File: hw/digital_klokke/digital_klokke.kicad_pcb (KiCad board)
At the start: 2 copper layers, 13 parts, among them SW101 SW_Push, SW102 SW_Push, SW103 SW_Push, U201 74LS47

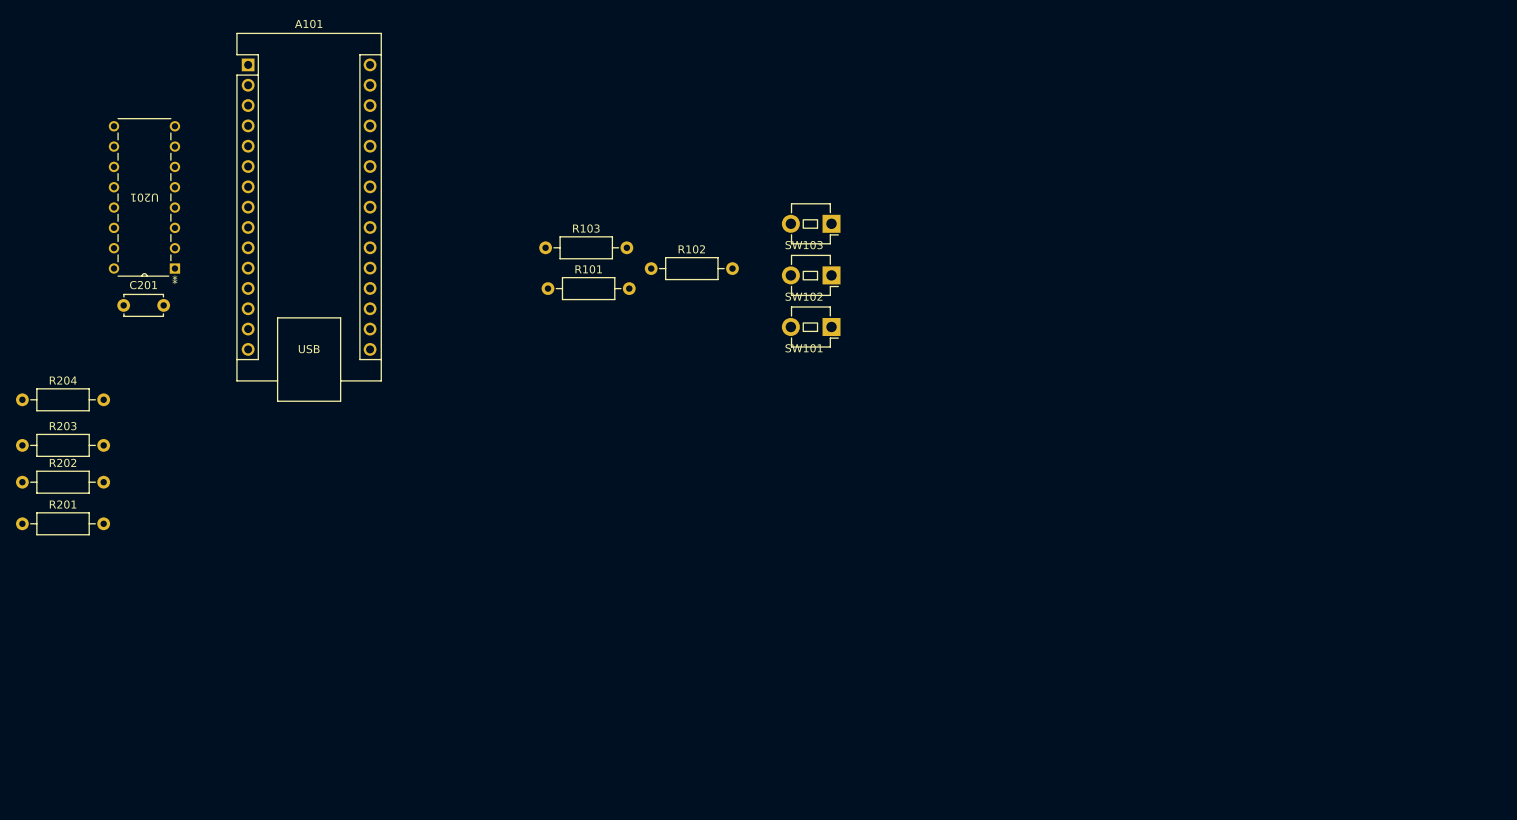
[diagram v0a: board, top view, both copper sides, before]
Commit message: added led for power indication. Started routing
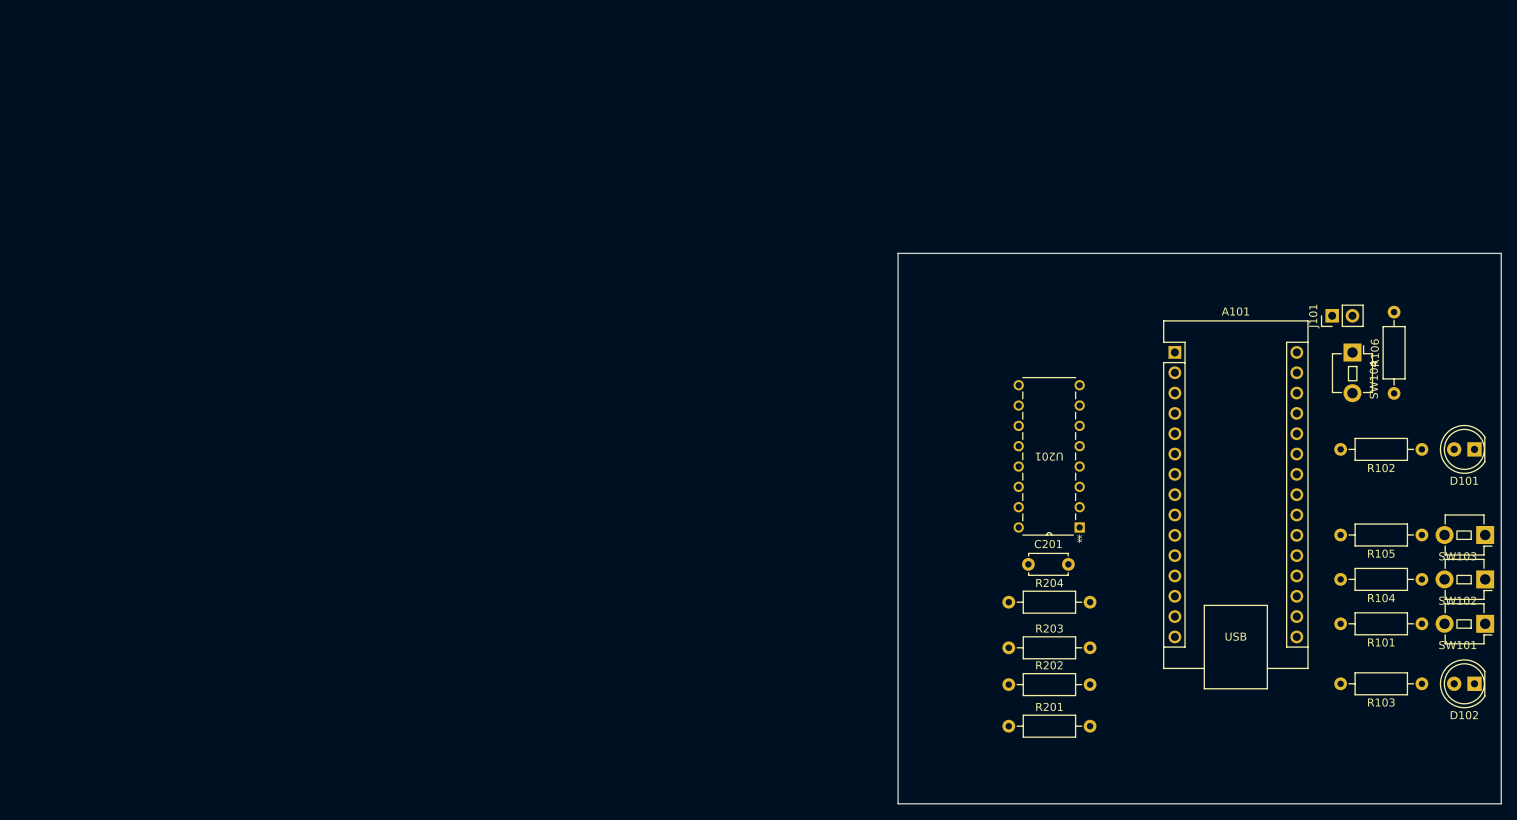
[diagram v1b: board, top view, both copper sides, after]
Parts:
- added D101: green, LED_THT:LED_D5.0mm, F.Cu at (210.4, 108.6)
- added D102: green, LED_THT:LED_D5.0mm, F.Cu at (210.4, 137.9)
- added J101: Conn_01x02_Pin, Connector_PinHeader_2.54mm:PinHeader_1x02_P2.54mm_Vertical, F.Cu at (192.6, 91.9)
- added R104: 1k, Resistor_THT:R_Axial_DIN0207_L6.3mm_D2.5mm_P10.16mm_Horizontal, F.Cu at (203.8, 124.8)
- added R105: 1k, Resistor_THT:R_Axial_DIN0207_L6.3mm_D2.5mm_P10.16mm_Horizontal, F.Cu at (203.8, 119.3)
- added R106: 1k, Resistor_THT:R_Axial_DIN0207_L6.3mm_D2.5mm_P10.16mm_Horizontal, F.Cu at (200.3, 101.6)
- added SW104: SW_Push, OMG_Switches:SW_PUSH_1P1T_6x3.5mm_H5.0_APEM_MJTP1250, F.Cu at (195.1, 96.5)
- R102: value 1k -> 270
- R103: value 1k -> 75
- moved R201 125.9 mm to (152.1, 143.2)
- moved R202 125.9 mm to (152.1, 138.0)
- moved R203 125.9 mm to (152.1, 133.4)
- moved R204 125.9 mm to (152.1, 127.7)
- moved R103 122.3 mm to (203.8, 137.9), turned to 180 degrees
- moved A101 121.3 mm to (172.9, 96.5)
- moved C201 117.6 mm to (154.6, 123.0)
- moved U201 117.6 mm to (153.4, 100.6)
- moved R101 117.0 mm to (203.8, 130.4), turned to 180 degrees
- moved R102 99.0 mm to (203.8, 108.6), turned to 180 degrees
- moved SW103 90.5 mm to (211.7, 119.3)
- moved SW102 90.1 mm to (211.7, 124.8)
- moved SW101 89.7 mm to (211.7, 130.4)
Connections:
- A101 pad 17: unconnected-(A101-3V3-Pad17) -> +3V3
- A101 pad 28: unconnected-(A101-~{RESET}-Pad28) -> /nRST
- A101 pad 3: unconnected-(A101-~{RESET}-Pad3) -> /nRST
- R102 pad 1: /Decrease_time -> Net-(D101-A)
- R102 pad 2: GND -> +5V
- R103 pad 1: /Adjust -> Net-(D102-A)
- R103 pad 2: GND -> +3V3
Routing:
- added copper zone on In2.Cu, net +5V
- added copper zone on In1.Cu, net GND
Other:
- board outline added: 75.4 x 68.8 mm
- copper layers 2 -> 4

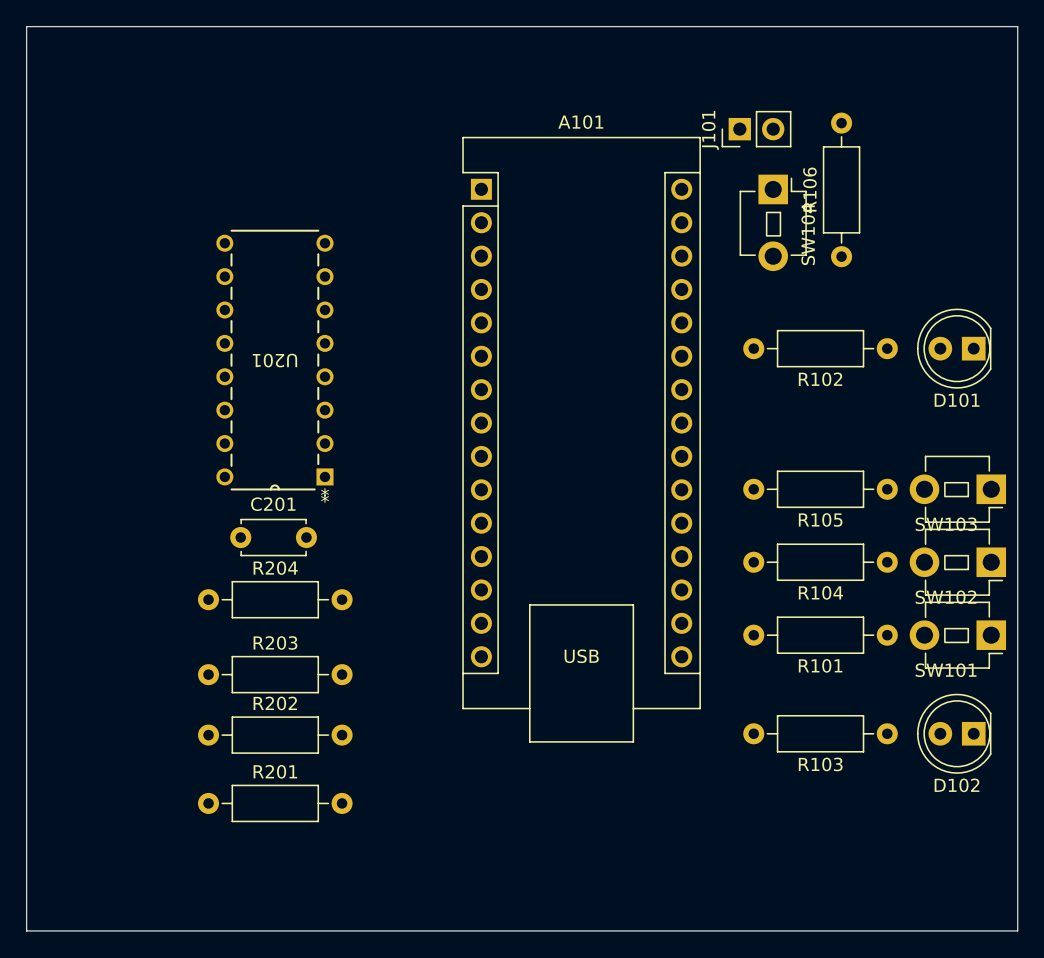
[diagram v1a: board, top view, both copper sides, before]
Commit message: added segment display footprint
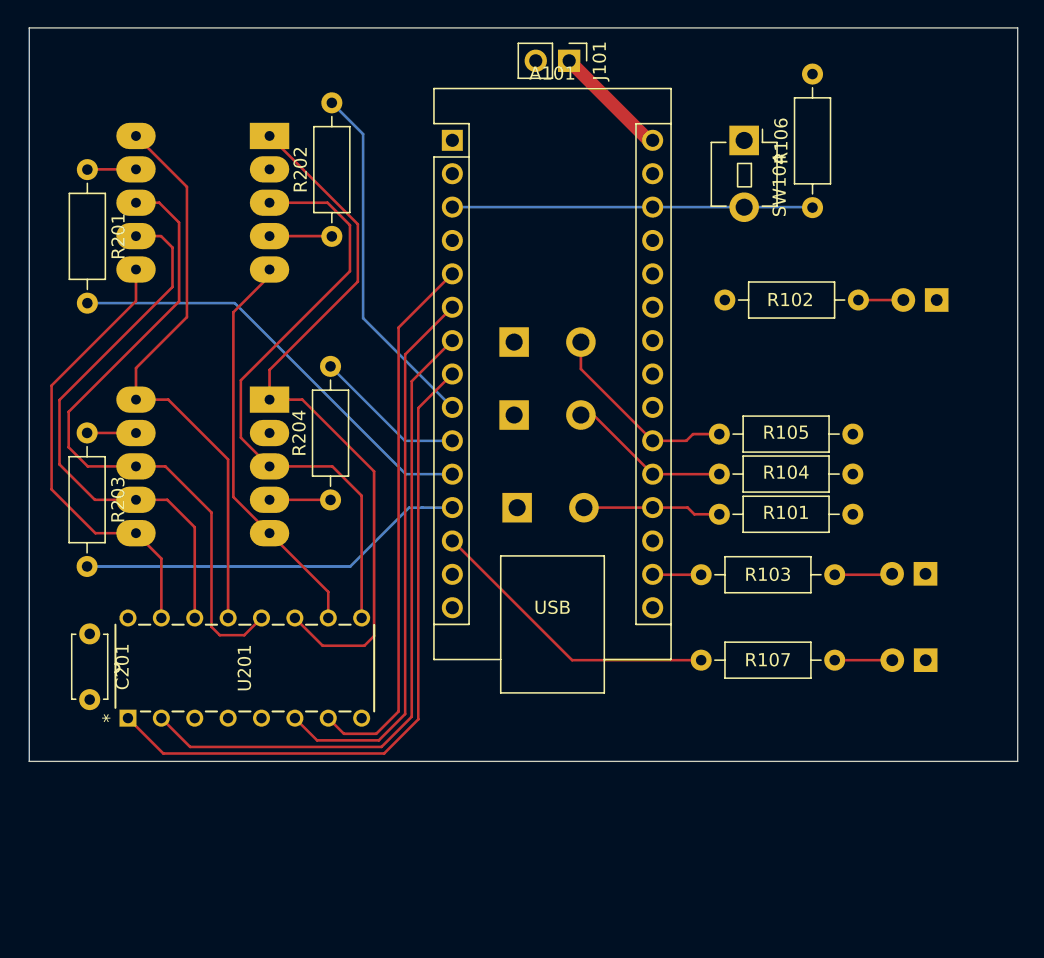
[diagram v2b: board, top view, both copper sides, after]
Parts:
- added D103: green, LED_THT:LED_D5.0mm, B.Cu at (206.7, 132.3)
- added D201: LTD-4608JF, OMG_Optoelectronics:Lite-On LTD-4608JF, B.Cu at (151.7, 97.5)
- added D202: LTD-4608JF, OMG_Optoelectronics:Lite-On LTD-4608JF, B.Cu at (151.7, 117.6)
- added R107: 270, Resistor_THT:R_Axial_DIN0207_L6.3mm_D2.5mm_P10.16mm_Horizontal, F.Cu at (199.8, 132.3)
- D101, D102, SW101, SW102, SW103: moved to B.Cu
- moved R201 49.1 mm to (142.9, 95.0), turned to -90 degrees
- moved R202 39.1 mm to (161.5, 100.1), turned to 90 degrees
- moved SW103 38.0 mm to (175.4, 108.1), turned to 0 degrees
- moved SW102 38.0 mm to (175.4, 113.7), turned to 0 degrees
- moved SW101 37.4 mm to (175.6, 120.7), turned to 0 degrees
- moved U201 30.4 mm to (163.8, 129.1), turned to 90 degrees
- moved R203 20.6 mm to (142.9, 115.0), turned to -90 degrees
- moved R101 15.7 mm to (191.0, 121.2), turned to 0 degrees
- moved R104 14.4 mm to (191.0, 118.1), turned to 0 degrees
- moved J101 14.0 mm to (179.6, 86.7), turned to -90 degrees
- moved C201 13.6 mm to (143.1, 130.3), turned to -90 degrees
- moved R105 13.5 mm to (191.0, 115.1), turned to 0 degrees
- moved R103 12.7 mm to (199.8, 125.8)
- moved D102 12.7 mm to (206.7, 125.7)
- moved R204 12.0 mm to (161.4, 120.1), turned to 90 degrees
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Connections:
- net /seven_segment/A renamed /A
- net /seven_segment/B renamed /B
- net /seven_segment/C renamed /C
- net /seven_segment/D renamed /D
- A101 pad 10: /seven_segment/Minutes_ones -> /Minutes_tens
- A101 pad 11: /seven_segment/Seconds_tens -> /Seconds_ones
- A101 pad 12: /seven_segment/Seconds_ones -> /Minutes_ones
- A101 pad 13: unconnected-(A101-D10-Pad13) -> /config_led
- A101 pad 9: /seven_segment/Minutes_tens -> /Seconds_tens
- R201 pad 2: /seven_segment/Seconds_ones -> /Seconds_ones
- R202 pad 2: /seven_segment/Seconds_tens -> /Seconds_tens
- R203 pad 2: /seven_segment/Minutes_ones -> /Minutes_ones
- R204 pad 2: /seven_segment/Minutes_tens -> /Minutes_tens
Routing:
- net Net-(D201-C): track 0.00 -> 55.6 mm
- net /B: track 0.00 -> 51.6 mm
- net /C: track 0.00 -> 50.8 mm
- net Net-(D201-B): track 0.00 -> 50.7 mm
- net Net-(D201-E): track 0.00 -> 46.8 mm
- net Net-(D201-A): track 0.00 -> 44.2 mm
- net Net-(D201-G): track 0.00 -> 42.4 mm
- net /D: track 0.00 -> 42.4 mm
- net /A: track 0.00 -> 41.5 mm
- net Net-(D201-F): track 0.00 -> 34.4 mm
- net /Seconds_ones: track 0.00 -> 33.2 mm
- net Net-(D201-D): track 0.00 -> 30.6 mm
- net /Minutes_ones: track 0.00 -> 29.6 mm
- net /nRST: track 0.00 -> 27.4 mm
- net /Seconds_tens: track 0.00 -> 27.0 mm
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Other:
- board size 75.4 x 68.8 mm -> 75.2 x 55.8 mm

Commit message: final design changes. Design freeze
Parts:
- removed D103: green, LED_THT:LED_D5.0mm
- removed R107: 270, Resistor_THT:R_Axial_DIN0207_L6.3mm_D2.5mm_P10.16mm_Horizontal
- added H101: MountingHole, MountingHole:MountingHole_4.3mm_M4, F.Cu at (348.5, 94.1)
- added H102: MountingHole, MountingHole:MountingHole_4.3mm_M4, F.Cu at (312.8, 135.2)
- moved SW101 164.6 mm to (340.2, 116.9), turned to 90 degrees
- moved SW102 158.5 mm to (333.9, 116.9), turned to 90 degrees
- moved SW103 152.5 mm to (327.6, 116.9), turned to 90 degrees
- moved R101 150.9 mm to (340.7, 102.5), turned to 90 degrees
- moved R104 147.5 mm to (337.6, 102.5), turned to 90 degrees
- moved A101 144.7 mm to (312.2, 122.9), turned to 90 degrees
- moved R105 144.1 mm to (334.6, 102.5), turned to 90 degrees
- moved R202 142.9 mm to (304.3, 104.4)
- moved C201 142.9 mm to (285.9, 134.6)
- moved D201 142.9 mm to (294.5, 101.8)
- moved D202 142.9 mm to (294.5, 121.9)
- moved R201 142.9 mm to (285.7, 99.3)
- moved R203 142.9 mm to (285.7, 119.3)
- moved R204 142.9 mm to (304.2, 124.4)
- moved U201 142.9 mm to (306.6, 133.4)
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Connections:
- D201 pad 2: +5V -> /config_led
- D202 pad 2: +5V -> /config_led
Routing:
- net /Minutes_ones: track 29.6 -> 117.1 mm
- net /Seconds_ones: track 33.2 -> 91.6 mm
- net /config_led: track 22.7 -> 76.0 mm
- net /Seconds_tens: track 27.0 -> 57.0 mm
- net +3V3: track 3.70 -> 30.9 mm
- net /Minutes_tens: track 11.6 -> 34.5 mm
- net /A: track 41.5 -> 32.7 mm
- net +9V: track 8.86 -> 16.6 mm
- net /B: track 51.6 -> 56.9 mm
- net Net-(D103-A): track 4.38 -> 0.00 mm
- net /D: track 42.4 -> 38.3 mm
- net +5V: track 0.00 -> 3.41 mm
- net Net-(D201-C): track 55.6 -> 57.5 mm
- net /nRST: track 27.4 -> 25.7 mm
- net /Decrease_time: track 12.4 -> 10.9 mm
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- added copper zone on B.Cu, net GND
- added copper zone on F.Cu, net GND
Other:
- board size 75.2 x 55.8 mm -> 73.1 x 55.8 mm
- board text added: "${TITLE} - ${REVISION}"
- board text added: "0"
- board text added: "0 mm"
- board text added: "0.0000 mm / 0.0000 mm"
- board text added: "0.01 mm"
- board text added: "0.02"
- board text added: "0.035 mm"
- board text added: "0.1 mm"
- board text added: "0.3000 mm"
- board text added: "1"
- board text added: "1.24 mm"
- board text added: "1.6000 mm"
- board text added: "3.3"
- board text added: "4"
- board text added: "4.5"
- board text added: "73.1000 mm x 55.8000 mm"
- board text added: "@omg_vustah"
- board text added: "B.Mask"
- board text added: "B.Paste"
- board text added: "B.Silkscreen"
- board text added: "BOARD CHARACTERISTICS"
- board text added: "Board Thickness:"
- board text added: "Board overall dimensions:"
- board text added: "Bottom Silk Screen"
- board text added: "Bottom Solder Mask"
- board text added: "Bottom Solder Paste"
- board text added: "Castellated pads:"
- board text added: "Color"
- board text added: "Copper Finish:"
- board text added: "Copper Layer Count:"
- board text added: "Dielectric 1"
- board text added: "Dielectric 2"
- board text added: "Dielectric 3"
- board text added: "Edge card connectors:"
- board text added: "Epsilon R"
- board text added: "F.Mask"
- board text added: "F.Paste"
- board text added: "F.Silkscreen"
- board text added: "FR4"
- board text added: "Impedance Control:"
- board text added: "L1_top"
- board text added: "L2_GND"
- board text added: "L3_PWR"
- board text added: "L4_bot"
- board text added: "Layer Name"
- board text added: "Loss Tangent"
- board text added: "Material"
- board text added: "Min hole diameter:"
- board text added: "Min track/spacing:"
- board text added: "No"
- board text added: "None"
- board text added: "Not specified"
- board text added: "Ole M.G. Vister"
- board text added: "Plated Board Edge:"
- board text added: "Thickness (mm)"
- board text added: "Top Silk Screen"
- board text added: "Top Solder Mask"
- board text added: "Top Solder Paste"
- board text added: "Type"
- board text added: "copper"
- board text added: "core"
- board text added: "prepreg"

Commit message: added resistor to each cathode
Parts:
- added R205: 470, Resistor_SMD:R_0805_2012Metric_Pad1.20x1.40mm_HandSolder, F.Cu at (304.2, 101.8)
- added R206: 470, Resistor_SMD:R_0805_2012Metric_Pad1.20x1.40mm_HandSolder, F.Cu at (284.9, 106.9)
- added R207: 470, Resistor_SMD:R_0805_2012Metric_Pad1.20x1.40mm_HandSolder, F.Cu at (284.9, 104.3)
- added R208: 470, Resistor_SMD:R_0805_2012Metric_Pad1.20x1.40mm_HandSolder, F.Cu at (304.2, 99.3)
- added R209: 470, Resistor_SMD:R_0805_2012Metric_Pad1.20x1.40mm_HandSolder, F.Cu at (284.9, 116.8)
- added R210: 470, Resistor_SMD:R_0805_2012Metric_Pad1.20x1.40mm_HandSolder, F.Cu at (284.9, 121.8)
- added R211: 470, Resistor_SMD:R_0805_2012Metric_Pad1.20x1.40mm_HandSolder, F.Cu at (304.2, 116.8)
- added R212: 470, Resistor_SMD:R_0805_2012Metric_Pad1.20x1.40mm_HandSolder, F.Cu at (304.2, 126.9)
- added R213: 470, Resistor_SMD:R_0805_2012Metric_Pad1.20x1.40mm_HandSolder, F.Cu at (304.2, 121.9)
- added R214: 470, Resistor_SMD:R_0805_2012Metric_Pad1.20x1.40mm_HandSolder, F.Cu at (284.9, 126.9)
- added R215: 470, Resistor_SMD:R_0805_2012Metric_Pad1.20x1.40mm_HandSolder, F.Cu at (284.9, 124.4)
- added R216: 470, Resistor_SMD:R_0805_2012Metric_Pad1.20x1.40mm_HandSolder, F.Cu at (304.2, 119.3)
- R101, R102, R103, R104, R105, R106, R201, R202, R203, R204: footprint Resistor_THT:R_Axial_DIN0207_L6.3mm_D2.5mm_P10.16mm_Horizontal -> Resistor_SMD:R_0805_2012Metric_Pad1.20x1.40mm_HandSolder
- moved R203 29.2 mm to (304.2, 96.7), turned to 180 degrees
- moved R202 19.6 mm to (284.9, 101.8), turned to 0 degrees
- moved R204 17.5 mm to (304.2, 106.9), turned to 180 degrees
- moved R201 2.71 mm to (284.9, 96.7), turned to 0 degrees
- moved R106 1.00 mm to (318.3, 97.2)
- moved R104 0.88 mm to (337.6, 101.6)
- moved R105 0.88 mm to (334.6, 101.6)
- moved R101 0.88 mm to (340.7, 101.6)
- moved R103 0.86 mm to (340.6, 135.4)
- moved R102 0.74 mm to (340.5, 128.8)
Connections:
- D201 pad 2: /config_led -> Net-(D201-DP)
- D201 pad 4: Net-(D201-Digit_2) -> /Seconds_tens
- D201 pad 9: Net-(D201-Digit_1) -> /Seconds_ones
- D202 pad 1: Net-(D201-C) -> Net-(D202-C)
- D202 pad 10: Net-(D201-A) -> Net-(D202-A)
- D202 pad 2: /config_led -> Net-(D202-DP)
- D202 pad 3: Net-(D201-E) -> Net-(D202-E)
- D202 pad 4: Net-(D202-Digit_2) -> /Minutes_tens
- D202 pad 5: Net-(D201-D) -> Net-(D202-D)
- D202 pad 6: Net-(D201-F) -> Net-(D202-F)
- D202 pad 7: Net-(D201-G) -> Net-(D202-G)
- D202 pad 8: Net-(D201-B) -> Net-(D202-B)
- D202 pad 9: Net-(D202-Digit_1) -> /Minutes_ones
- R201 pad 1: Net-(D201-Digit_1) -> Net-(U201-a)
- R201 pad 2: /Seconds_ones -> Net-(D201-A)
- R202 pad 1: Net-(D201-Digit_2) -> Net-(U201-b)
- R202 pad 2: /Seconds_tens -> Net-(D201-B)
- R203 pad 1: Net-(D202-Digit_1) -> Net-(U201-c)
- R203 pad 2: /Minutes_ones -> Net-(D201-C)
- R204 pad 1: Net-(D202-Digit_2) -> Net-(U201-d)
- R204 pad 2: /Minutes_tens -> Net-(D201-D)
- U201 pad 10: Net-(D201-D) -> Net-(U201-d)
- U201 pad 11: Net-(D201-C) -> Net-(U201-c)
- U201 pad 12: Net-(D201-B) -> Net-(U201-b)
- U201 pad 13: Net-(D201-A) -> Net-(U201-a)
- U201 pad 14: Net-(D201-G) -> Net-(U201-g)
- U201 pad 15: Net-(D201-F) -> Net-(U201-f)
- U201 pad 9: Net-(D201-E) -> Net-(U201-e)
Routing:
- net /config_led: track 76.0 -> 0.00 mm
- net Net-(U201-a): track 0.00 -> 60.7 mm
- net /Minutes_ones: track 117.1 -> 61.3 mm
- net Net-(D201-C): track 57.5 -> 3.65 mm
- net Net-(D201-B): track 50.7 -> 3.52 mm
- net Net-(D201-E): track 46.8 -> 3.65 mm
- net Net-(D201-A): track 44.2 -> 3.53 mm
- net Net-(D201-G): track 42.4 -> 3.52 mm
- net Net-(U201-g): track 0.00 -> 36.9 mm
- net Net-(U201-f): track 0.00 -> 32.1 mm
- net Net-(D201-F): track 34.4 -> 3.52 mm
- net Net-(D201-D): track 30.6 -> 3.65 mm
- net /Seconds_ones: track 91.6 -> 78.8 mm
- net Net-(U201-b): track 0.00 -> 12.3 mm
- net /Seconds_tens: track 57.0 -> 50.5 mm
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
